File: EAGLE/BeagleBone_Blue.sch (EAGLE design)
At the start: 303 parts, among them J2 SERVO_HEADERS_8X, M1 JST_ZH_2, M2 JST_ZH_2, M3 JST_ZH_2, M4 JST_ZH_2, Q1 MOSFET-N, T1 BSS138W-7-F, T2 BSS138W-7-F, U1 TCAN1051HV, U10 TXS0108ERGYR, U13 EMMC, U2 SN74LV1T126DBVR, U3 TPD4S012DRY, U4 TPD4S012DRY, U5 24LC_32AT-I/OT, U6 SN74LVC1G07_DCK_5, U7 WL1835MODGBMOCT, U9 TXS0108ERGYR, X2 SCHA5B0200, X3 USB1, X4 10118192-0001LF, Y1 24 MHz, Y2 32.768kHz

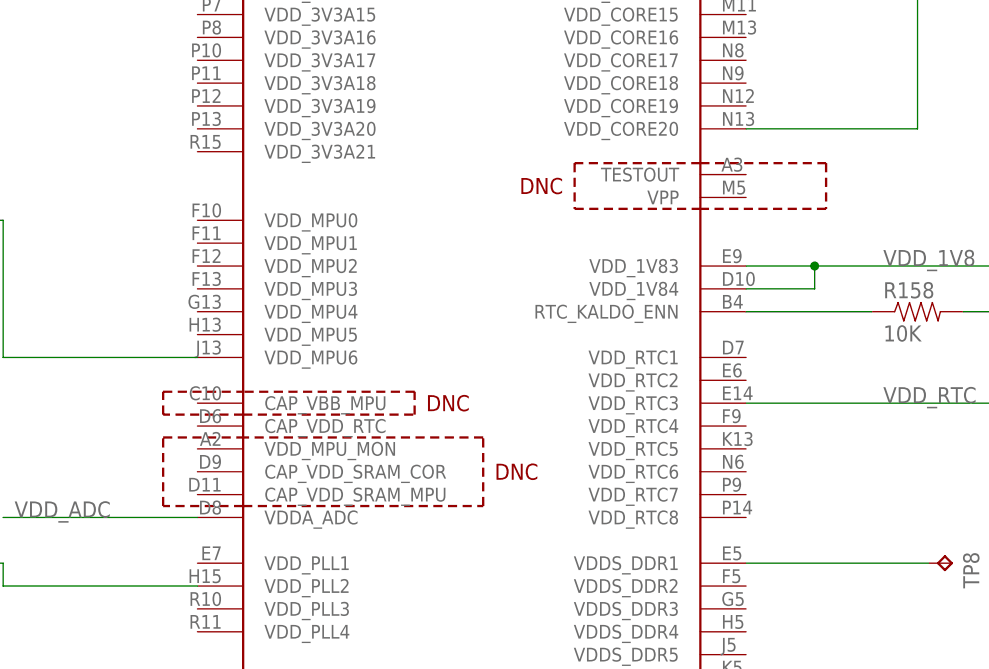
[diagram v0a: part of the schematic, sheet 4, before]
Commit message: EAGLE: more attempts to consolidate library
I tried to rename some parts to eliminate the prefixes added by the exp-lbrs.ulp script.
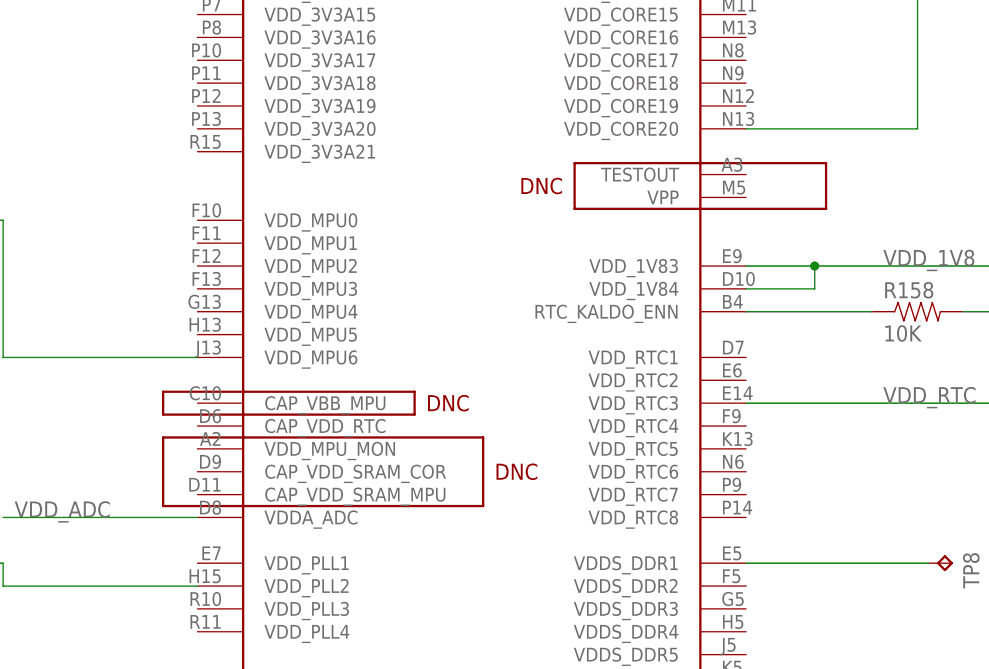
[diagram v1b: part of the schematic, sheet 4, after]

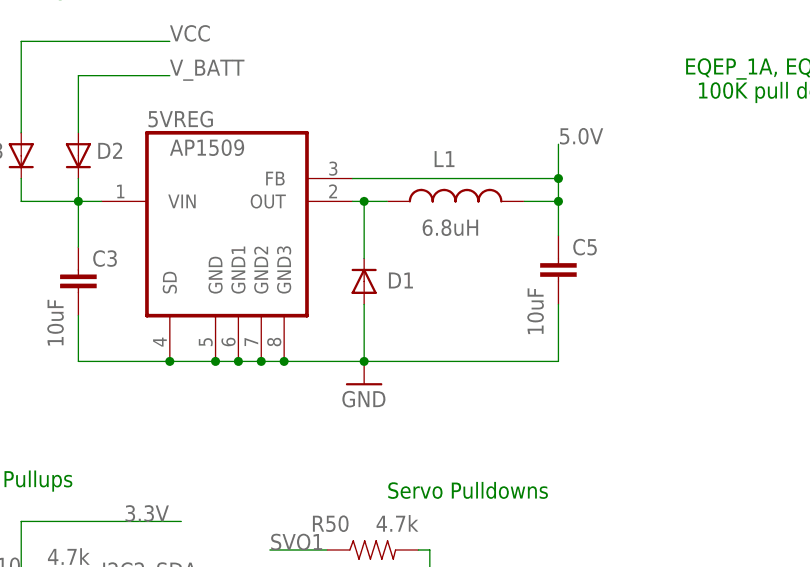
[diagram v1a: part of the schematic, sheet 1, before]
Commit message: BRD: update D1, D2, D3 footprints
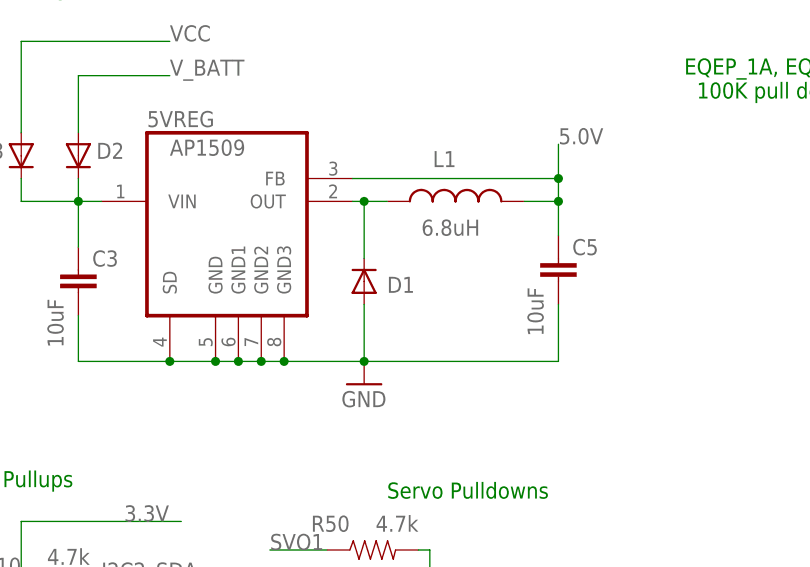
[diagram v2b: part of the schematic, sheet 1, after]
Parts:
- D1: device adafruit:DIODESOD-123 -> BeagleBone_Blue:DIODE_SOD-123FL
- D2, D3: device adafruit:DIODESOD-123 -> adafruit:DIODE_SOD-123FL
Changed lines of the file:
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@@
 <setting verticaltext="up"/>
 </settings>
-<grid distance="0.1" unitdist="inch" unit="inch" style="lines" multiple="1" display="no" altdistance="0.01" altunitdist="inch" altunit="inch"/>
+<grid distance="0.05" unitdist="inch" unit="inch" style="lines" multiple="1" display="no" altdistance="0.01" altunitdist="inch" altunit="inch"/>
 <layers>
 <layer number="1" name="Top" color="4" fill="1" visible="yes" active="no"/>
@@
 <part name="GND18" library="SparkFun" deviceset="GND" device=""/>
 <part name="GND6" library="SparkFun-Aesthetics" deviceset="GND" device=""/>
-<part name="D1" library="adafruit" deviceset="DIODE" device="SOD-123"/>
-<part name="D2" library="adafruit" deviceset="DIODE" device="SOD-123"/>
+<part name="D2" library="adafruit" deviceset="DIODE" device="_SOD-123FL"/>
 <part name="CHG" library="SparkFun-LED" deviceset="LED" device="0603" value="GRN"/>
 <part name="R3" library="Strawson_Eagle_Lib" deviceset="RESISTOR" device="0402-RES" value="1k"/>
@@
 <part name="R5" library="Strawson_Eagle_Lib" deviceset="RESISTOR" device="0402-RES" value="10k"/>
 <part name="R6" library="Strawson_Eagle_Lib" deviceset="RESISTOR" device="0402-RES" value="10k"/>
-<part name="D3" library="adafruit" deviceset="DIODE" device="SOD-123"/>
+<part name="D3" library="adafruit" deviceset="DIODE" device="_SOD-123FL"/>
 <part name="GND12" library="SparkFun" deviceset="GND" device=""/>
 <part name="GND14" library="SparkFun" deviceset="GND" device=""/>
@@
 <part name="TP8" library="BeagleBone_Blue" deviceset="TP" device="B0,65"/>
 <part name="12V" library="GHI" deviceset="PJ-102B_POWER_CON" device=""/>
+<part name="D1" library="BeagleBone_Blue" deviceset="DIODE" device="_SOD-123FL"/>
 </parts>
 <sheets>
@@
 <instance part="GND18" gate="1" x="107.95" y="156.21"/>
 <instance part="GND6" gate="1" x="194.31" y="102.87"/>
-<instance part="D1" gate="G$1" x="194.31" y="114.3" smashed="yes" rot="R90">
-<attribute name="NAME" x="196.85" y="113.5126" size="1.778" layer="95"/>
-</instance>
 <instance part="D2" gate="G$1" x="162.56" y="128.27" smashed="yes" rot="R270">
 <attribute name="NAME" x="167.64" y="129.6924" size="1.778" layer="95" rot="R180"/>
@@
 <instance part="SUPPLY86" gate="G$1" x="350.52" y="127" rot="MR0"/>
 <instance part="12V" gate="G$1" x="373.38" y="137.16" smashed="yes" rot="MR0"/>
+<instance part="D1" gate="G$1" x="194.31" y="114.3" smashed="yes" rot="R90">
+<attribute name="NAME" x="196.85" y="113.03" size="1.778" layer="95"/>
+<attribute name="VALUE" x="198.12" y="111.76" size="1.27" layer="96" rot="R90"/>
+</instance>
 </instances>
 <busses>
@@
 <net name="N$16" class="0">
 <segment>
-<pinref part="D1" gate="G$1" pin="C"/>
 <pinref part="L1" gate="G$1" pin="1"/>
 <wire x1="196.85" y1="123.19" x2="194.31" y2="123.19" width="0.1524" layer="91"/>
@@
 <junction x="194.31" y="123.19"/>
 <pinref part="5VREG" gate="G$1" pin="OUT"/>
+<pinref part="D1" gate="G$1" pin="C"/>
 </segment>
 </net>
@@
 <wire x1="162.56" y1="105.41" x2="162.56" y2="110.49" width="0.1524" layer="91"/>
 <wire x1="215.9" y1="105.41" x2="194.31" y2="105.41" width="0.1524" layer="91"/>
-<pinref part="D1" gate="G$1" pin="A"/>
 <wire x1="194.31" y1="111.76" x2="194.31" y2="105.41" width="0.1524" layer="91"/>
 <pinref part="C3" gate="G$1" pin="2"/>
@@
 <pinref part="5VREG" gate="G$1" pin="SD"/>
 <junction x="172.72" y="105.41"/>
-</segment>
-<segment>
+<pinref part="D1" gate="G$1" pin="A"/>
+</segment>
+<segment>

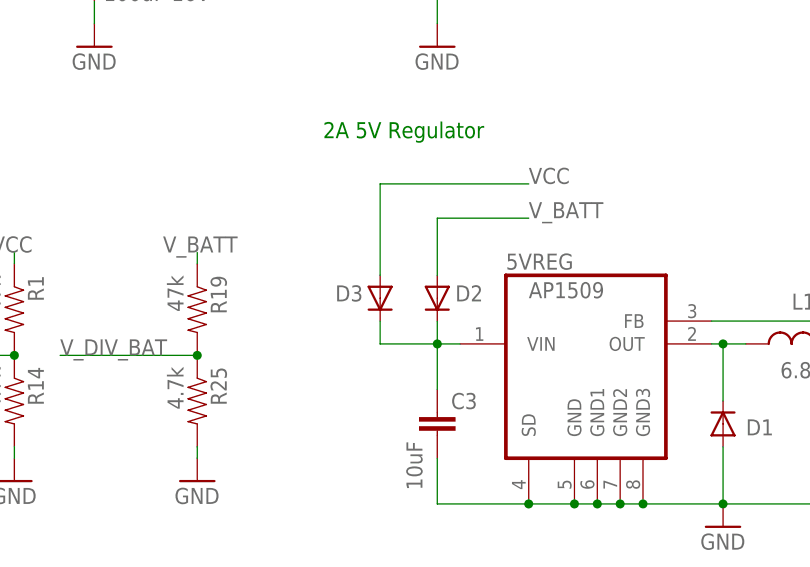
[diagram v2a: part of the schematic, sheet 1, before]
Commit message: Fixing silkscreen issues.
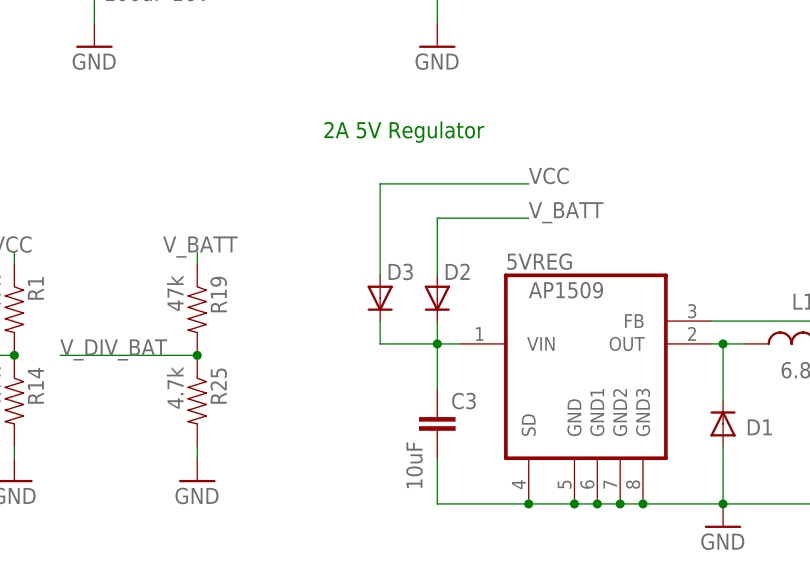
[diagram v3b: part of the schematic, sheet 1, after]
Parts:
- D2, D3: device adafruit:DIODE_SOD-123FL -> BeagleBone_Blue:DIODE_SOD-123FL

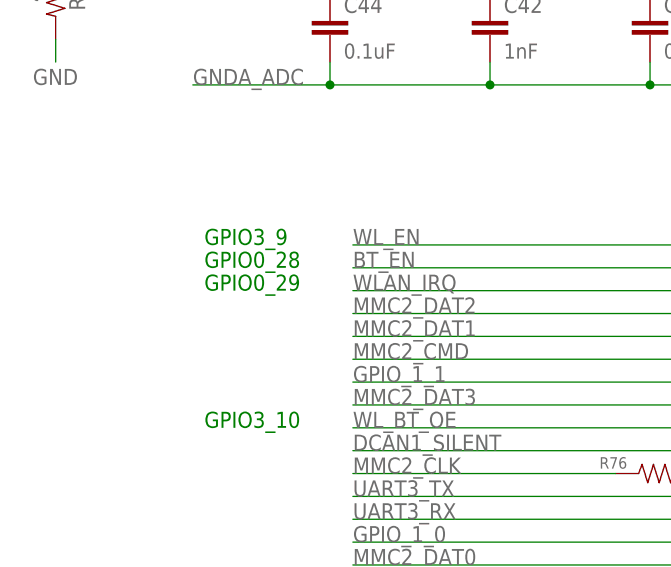
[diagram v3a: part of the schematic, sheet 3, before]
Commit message: Fix WL_IRQ GPIO note
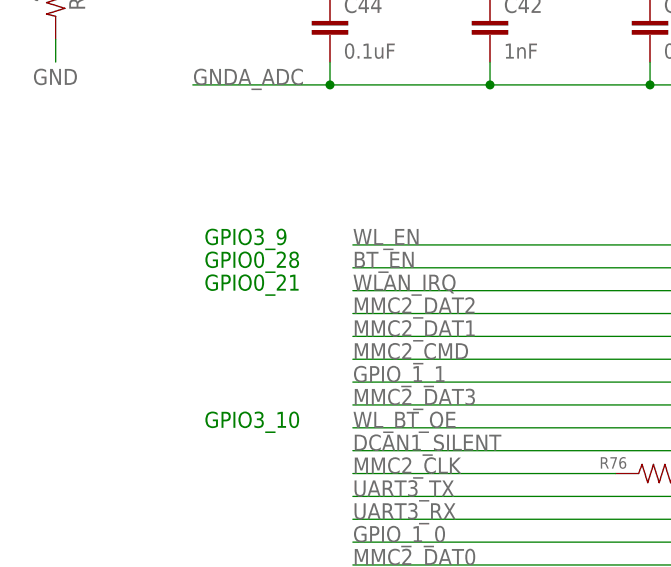
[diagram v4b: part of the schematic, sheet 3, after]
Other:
- note added: "GPIO0_21"
- note removed: "GPIO0_29"
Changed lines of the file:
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@@
 <setting verticaltext="up"/>
 </settings>
-<grid distance="0.05" unitdist="inch" unit="inch" style="lines" multiple="1" display="no" altdistance="0.01" altunitdist="inch" altunit="inch"/>
+<grid distance="0.1" unitdist="inch" unit="inch" style="lines" multiple="1" display="no" altdistance="0.01" altunitdist="inch" altunit="inch"/>
 <layers>
 <layer number="1" name="Top" color="4" fill="1" visible="no" active="no"/>
@@
 <text x="57.15" y="144.78" size="1.778" layer="91">GPIO3_9</text>
 <text x="57.15" y="142.24" size="1.778" layer="91">GPIO0_28</text>
-<text x="57.15" y="139.7" size="1.778" layer="91">GPIO0_29</text>
+<text x="57.15" y="139.7" size="1.778" layer="91">GPIO0_21</text>
 <text x="57.15" y="124.46" size="1.778" layer="91">GPIO3_10</text>
 </plain>

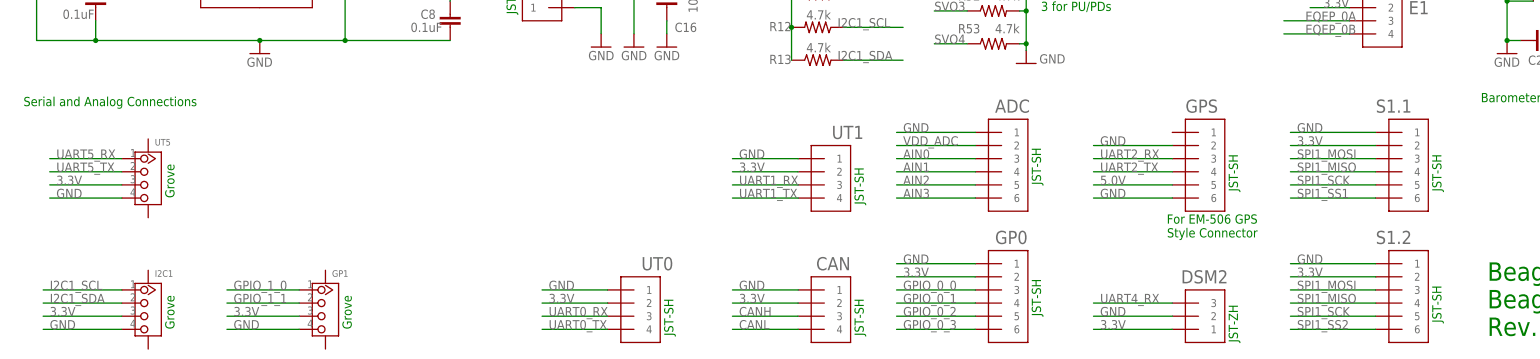
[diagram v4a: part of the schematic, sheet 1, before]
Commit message: Schematic updates for Rev A2.  See Issues.
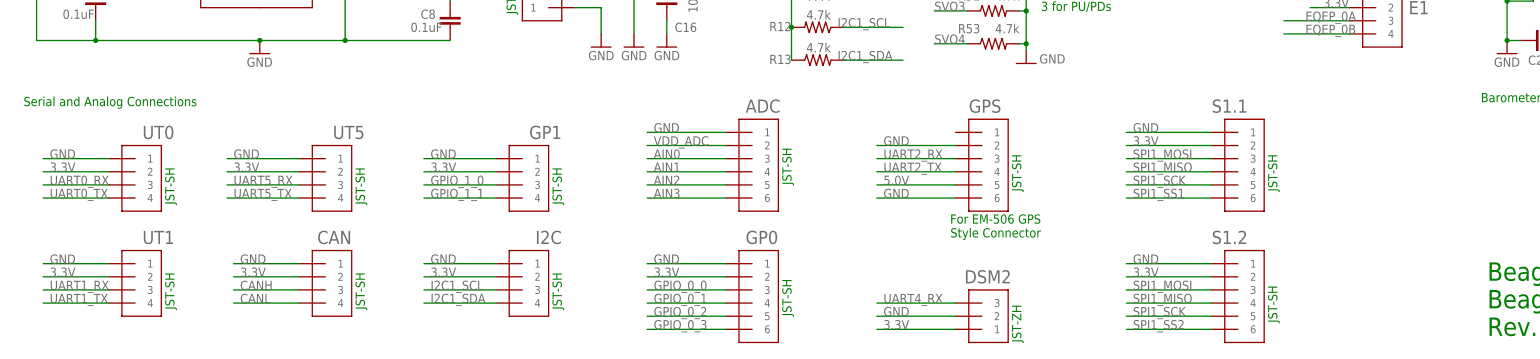
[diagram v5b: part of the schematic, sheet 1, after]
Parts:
- removed BT, WL: BLUE, BeagleBone_Blue:LED0603
- removed I2C1: H4P-SMD-2.0, Seeed-Connector -2016:GROVE-CONNECTOR-SMD(4+2P-2.0)
- removed R95: 1K, Strawson_Eagle_Lib:RESISTOR0402-RES
- removed T1, T2: BSS138W-7-F, GHI Transistors:BSS138W-7-F
- added C59, C60: 10uF, SparkFun-Capacitors:CAP0805
- added GND: TESTPAD/W_HOLE_1X1, GHI2:TESTPAD/W_HOLE_1X1
- added I2C: JST_SH_4, Strawson_Eagle_Lib:JST_SH_4
- added WIFI: GREEN, BeagleBone_Blue:LED0603
- GP1, UT5: value H4P-SMD-2.0 -> JST_SH_4; device Seeed-Connector -2016:GROVE-CONNECTOR-SMD(4+2P-2.0) -> Strawson_Eagle_Lib:JST_SH_4
- R91: value 1K -> 240
- renumbered TP10 to WP
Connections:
- removed net N$44: R91.2, WL.C
- removed net N$46: BT.C, R95.2
- removed net N$64: R91.1, T1.D
- removed net N$68: R95.1, T2.D
- new net N$20: R91.1, WIFI.C
- new net WIFI_LED: SIPB.GPIO0_19_A15, WIFI.A
- net 3.3V: now also C59.1, GP1.2, I2C.2, UT5.2; no longer BT.A, GP1.3, I2C1.3, UT5.3, WL.A
- net 5.0V: no longer U1.VCC
- net BT_EN_1V8: no longer T2.G
- net GND: now also C59.2, C60.1, GND.TP, GP1.1, I2C.1, R91.2, UT5.1; no longer GP1.4, I2C1.4, T1.S, T2.S, UT5.4
- net GPIO_0_3: now also SIPB.SPI1_CS0_C12; no longer SIPB.GPIO0_7_C18
- net GPIO_1_0: now also GP1.3; no longer GP1.1
- net GPIO_1_1: now also GP1.4; no longer GP1.2
- net I2C1_SCL: now also I2C.3; no longer I2C1.1
- net I2C1_SDA: now also I2C.4; no longer I2C1.2
- net MDIR_2B: now also R140.1, SIPC.LCD_DATA14_V4; no longer R131.2, SIPC.LCD_DATA9_U2
- net SPI1_SS1: now also SIPC.H18; no longer SIPB.SPI1_CS0_C12
- net SPI1_SS2: now also SIPB.GPIO0_7_C18; no longer SIPB.GPIO0_19_A15
- net SYS_5V: now also U1.VCC
- net UART5_RX: now also R131.2, SIPC.LCD_DATA9_U2, UT5.3; no longer R140.1, SIPC.LCD_DATA14_V4, UT5.1
- net UART5_TX: now also UT5.4; no longer UT5.2
- net VDD_1V8: now also C60.2
- net WL_EN_1V8: no longer T1.G
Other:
- note removed: "Grove"
- moved on the sheet: ADC, CAN, DSM2, GP0, GPS, R91, S1.1, S1.2, UT0, UT1
